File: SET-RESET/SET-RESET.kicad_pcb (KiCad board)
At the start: 2 copper layers, 100.1 x 100.1 mm, 107 parts, among them J1 BMS, J2 BSPD, J3 IMD, J4 IMD_SHTDNW, J5 BMS_SHTDNW, J6 BSPD_SHTDNW, J7 Led's paineis, J8 voltage supply, K1 RELAY_19.1x15.5mm, K2 RELAY_19.1x15.5mm, K3 RELAY_19.1x15.5mm, K4 RELAY_19.1x15.5mm, K5 RELAY_19.1x15.5mm, K6 RELAY_19.1x15.5mm, Q1 BC557, Q10 BC548, Q11 BC548, Q12 BC557, Q13 BC548, Q14 BC548, Q15 BC557, Q16 BC548, Q17 BC548, Q18 BC557, Q2 BC557, Q3 BC557, Q4 Si2302DS, Q5 Si2302DS, Q6 Si2302DS, Q7 BC548, Q8 BC548, Q9 BC548, U1 TLP290-4

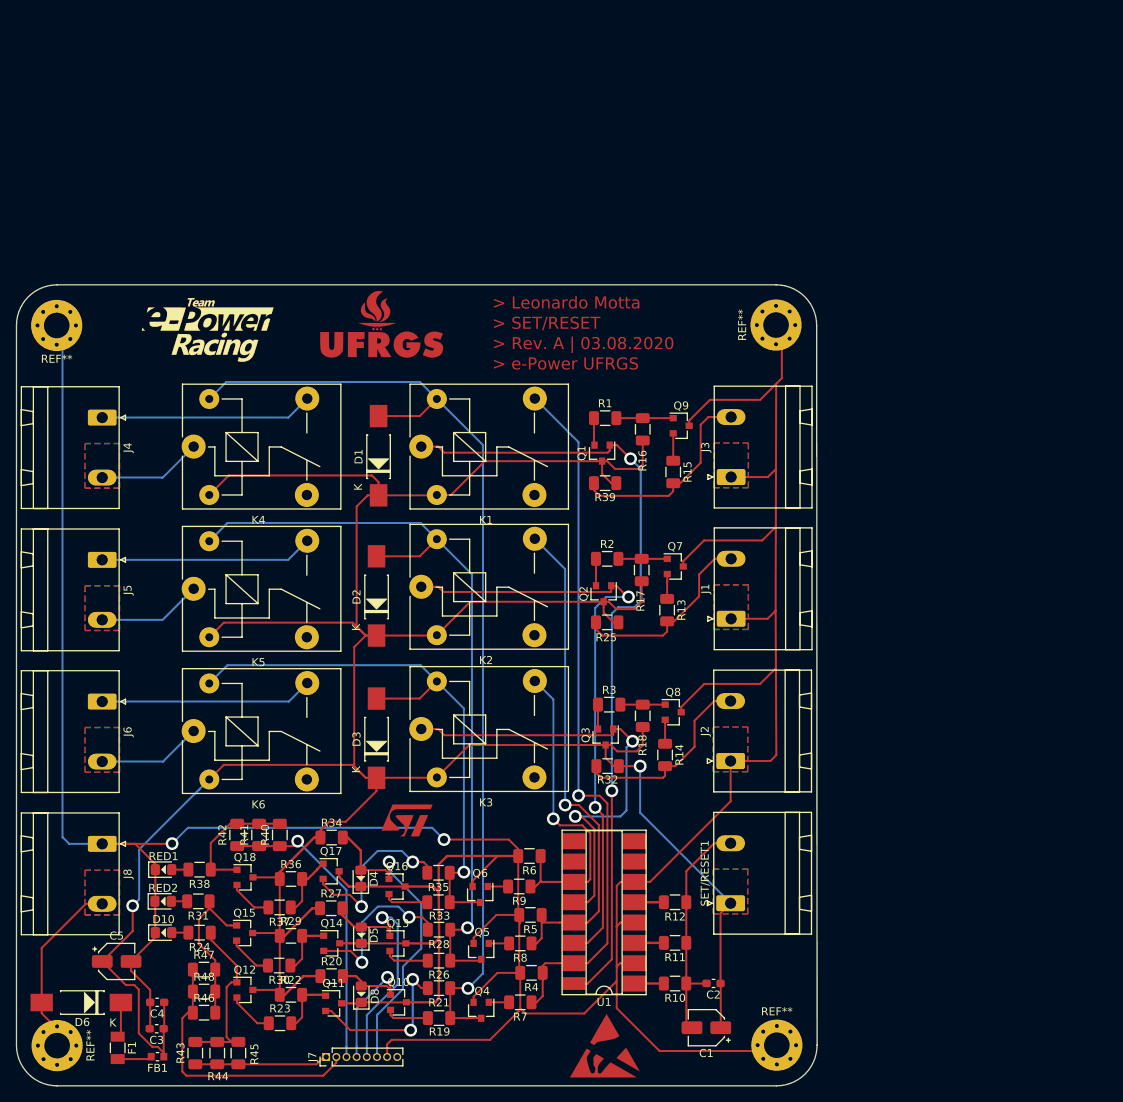
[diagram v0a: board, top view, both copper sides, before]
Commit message: Rev. B - BSPD and Rev. B - Set/Reset
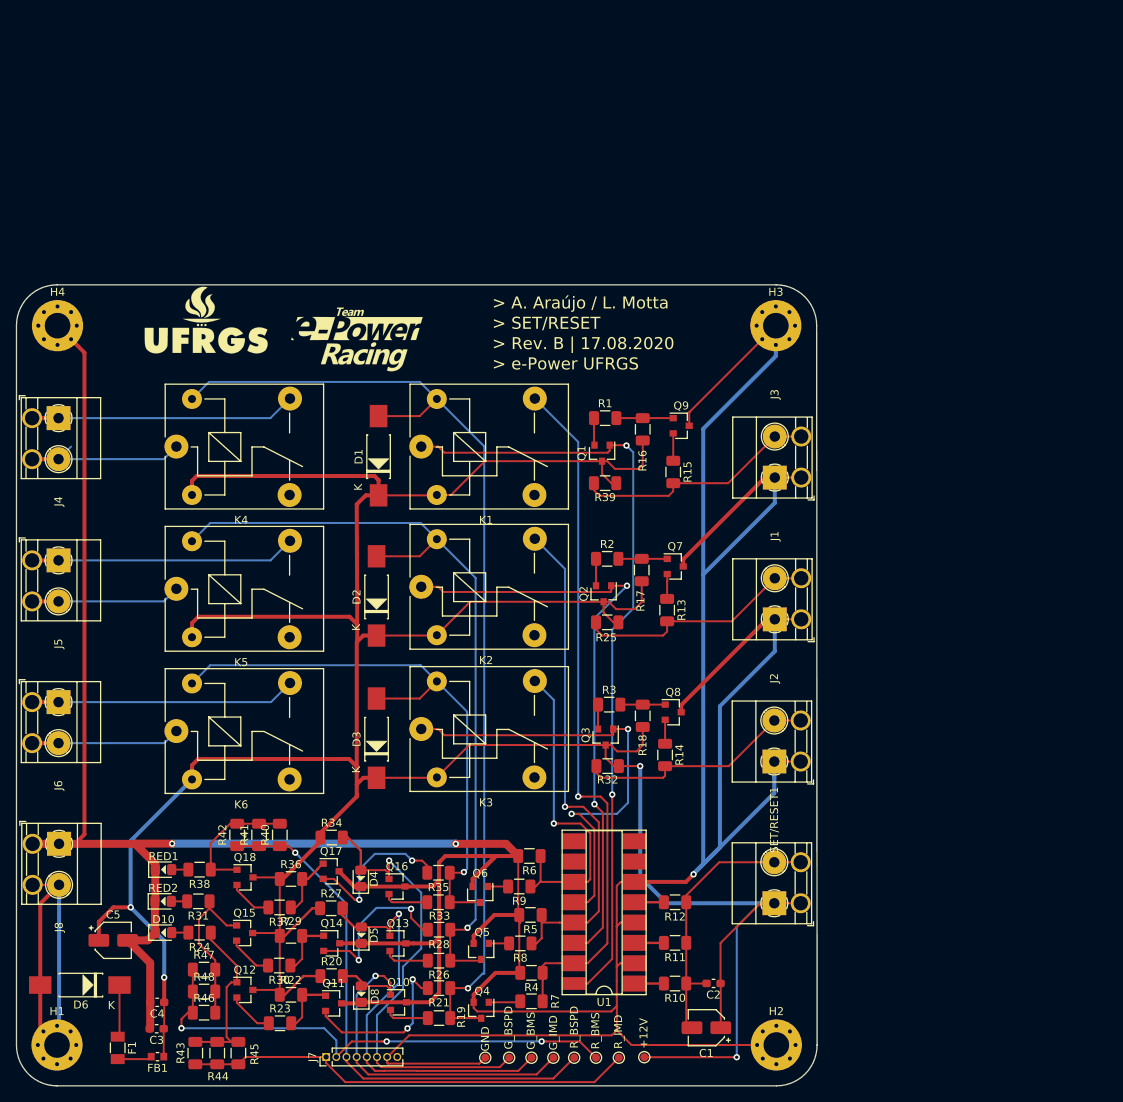
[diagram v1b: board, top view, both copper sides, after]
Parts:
- removed G3: ST Logo, e-Power:ST_6.5x4.1mm_Copper
- removed G4: UFRGS_1_14.7x8.0mm_Copper, e-Power:UFRGS_14.7x8.0mm_Copper
- removed REF** (x4): MountingHole_3.2mm_M3_Pad_Via, e-Power:MountingHole_3.2mm_M3_Pad_Via
- added G_BMS1: G_BMS, e-Power:TestPoint_Pad_D1.0mm, F.Cu at (177.4, 155.1)
- added G_BSPD1: G_BSPD, e-Power:TestPoint_Pad_D1.0mm, F.Cu at (174.6, 155.1)
- added G_IMD1: G_IMD, e-Power:TestPoint_Pad_D1.0mm, F.Cu at (180.1, 155.1)
- added H1: MountingHole_Pad, e-Power:MountingHole_3.2mm_M3_Pad_Via, F.Cu at (118.0, 153.5)
- added H2: MountingHole_Pad, e-Power:MountingHole_3.2mm_M3_Pad_Via, F.Cu at (208.0, 153.5)
- added H3: MountingHole_Pad, e-Power:MountingHole_3.2mm_M3_Pad_Via, F.Cu at (207.9, 63.6)
- added H4: MountingHole_Pad, e-Power:MountingHole_3.2mm_M3_Pad_Via, F.Cu at (118.1, 63.6)
- added R_BMS1: R_BMS, e-Power:TestPoint_Pad_D1.0mm, F.Cu at (185.4, 155.1)
- added R_BSPD1: R_BSPD, e-Power:TestPoint_Pad_D1.0mm, F.Cu at (182.7, 155.1)
- added R_IMD1: R_IMD, e-Power:TestPoint_Pad_D1.0mm, F.Cu at (188.3, 155.1)
- added TP1: GND, e-Power:TestPoint_Pad_D1.0mm, F.Cu at (171.6, 155.1)
- added TP2: +12V, e-Power:TestPoint_Pad_D1.0mm, F.Cu at (191.5, 155.1)
- C5: value 470uF -> 220uF
- G1: value e-Power_12.4x6.0mm_Copper -> Logo_e-Power_Large; footprint e-Power:e-Power_16.5x8.0mm_Copper -> e-Power:Logo_e-Power_16.5x8.0mm_SilkS
- G2: value UFRGS_1_11.0x6.0mm_Copper -> Logo_UFRGS_Large; footprint e-Power:ESD-Logo_8.9x8mm_Copper -> e-Power:Logo_UFRGS_14.7x8.0mm_SilkS
- J1, J2, J3, J4, J5, J6, J8, SET/RESET1: footprint Connector_Phoenix_GMSTB:PhoenixContact_GMSTBA_2,5_2-G_1x02_P7.50mm_Horizontal -> e-Power:TerminalBlock_Phoenix_MKDS-1,5-2_1x02_P5.08mm_Horizontal
- moved G2 103.5 mm to (136.7, 62.9)
- moved G1 18.7 mm to (155.5, 65.3)
- moved J4 5.46 mm to (118.2, 75.2)
- moved J5 5.46 mm to (118.2, 93.0)
- moved J6 5.46 mm to (118.2, 110.7)
- moved J1 5.46 mm to (207.8, 100.3)
- moved J2 5.46 mm to (207.7, 118.1)
- moved J3 5.46 mm to (207.8, 82.6)
- moved SET/RESET1 5.46 mm to (207.7, 135.8)
- moved J8 5.40 mm to (118.3, 128.4)
- moved C5 2.68 mm to (125.1, 140.5)
- moved D6 2.19 mm to (124.8, 146.1)
- moved K4 2.16 mm to (133.0, 78.7)
- moved K5 2.16 mm to (133.0, 96.5)
- moved K6 2.16 mm to (133.0, 114.3)
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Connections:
- D6 pad 2: +12V -> Input_Power
- J8 pad 2: +12V -> Input_Power
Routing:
- net GND: track 476.7 -> 587.9 mm, vias 2 -> 3
- net Input_Power: track 0.00 -> 44.9 mm
- net /ledRED_IMD: track 16.7 -> 56.3 mm
- net +12V: track 405.2 -> 435.3 mm, vias 2 -> 4
- net /ledRED_BMS: track 34.5 -> 64.5 mm, vias 0 -> 3
- net /ledRED_BSPD: track 37.3 -> 66.8 mm
- net /ledGREEN_IMD: track 21.5 -> 48.6 mm
- net /ledGREEN_BMS: track 30.8 -> 52.8 mm
- net /ledGREEN_BSPD: track 40.3 -> 58.5 mm
- net Net-(J5-Pad1): track 26.6 -> 35.4 mm
- net Net-(J4-Pad1): track 26.6 -> 35.4 mm
- net Net-(J6-Pad1): track 26.6 -> 35.4 mm
- net Net-(J4-Pad2): track 13.0 -> 20.9 mm
- net Net-(J1-Pad2): track 25.1 -> 31.4 mm
- net Net-(C1-Pad2): track 29.4 -> 35.4 mm
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- removed copper zone on B.Cu, net (none)
- removed copper zone on F.Cu, net (none)
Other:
- board text added: "> A. Araújo / L. Motta"
- board text added: "> Rev. B | 17.08.2020"
- board text removed: "> Leonardo Motta"
- board text removed: "> Rev. A | 03.08.2020"

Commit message: Set/Reset Rev. C
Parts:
- removed D10: RED, e-Power:LED_0805_1.15x1.40mm_HandSolder
- removed G_BMS1: G_BMS, e-Power:TestPoint_Pad_D1.0mm
- removed G_BSPD1: G_BSPD, e-Power:TestPoint_Pad_D1.0mm
- removed G_IMD1: G_IMD, e-Power:TestPoint_Pad_D1.0mm
- removed R40, R41, R42, R43, R44, R45, R46, R47, R48: 1K, Resistor_SMD:R_1206_3216Metric
- removed R_BMS1: R_BMS, e-Power:TestPoint_Pad_D1.0mm
- removed R_BSPD1: R_BSPD, e-Power:TestPoint_Pad_D1.0mm
- removed R_IMD1: R_IMD, e-Power:TestPoint_Pad_D1.0mm
- added RED3: RED, e-Power:LED_0805_1.15x1.40mm_HandSolder, F.Cu at (170.5, 121.0)
- added TP10: +VIN, e-Power:TestPoint_Pad_D1.0mm, F.Cu at (160.5, 123.4)
- added TP11: GND, e-Power:TestPoint_Pad_D1.0mm, F.Cu at (165.3, 123.4)
- added TP3: ERROR_BMS, e-Power:TestPoint_Pad_D1.0mm, F.Cu at (237.7, 40.2)
- added TP4: ERROR_IMD, e-Power:TestPoint_Pad_D1.0mm, F.Cu at (237.7, 37.9)
- added TP5: ERROR_BSPD, e-Power:TestPoint_Pad_D1.0mm, F.Cu at (237.8, 42.6)
- added TP7: Led_BSPD, e-Power:TestPoint_Pad_D1.0mm, F.Cu at (175.3, 114.2)
- added TP8: Led_IMD, e-Power:TestPoint_Pad_D1.0mm, F.Cu at (170.5, 114.2)
- added TP9: Led_BMS, e-Power:TestPoint_Pad_D1.0mm, F.Cu at (172.9, 114.2)
- C1, C5: footprint Capacitor_SMD:CP_Elec_4x5.3 -> Capacitor_SMD:CP_Elec_8x10
- C2, C3, C4: footprint Capacitor_SMD:C_0603_1608Metric_Pad1.05x0.95mm_HandSolder -> Capacitor_SMD:C_0805_2012Metric
- D1, D2, D3, D6: value 1N5819 -> SS54HF; footprint e-Power:DO-41_SMD -> e-Power:DO-214AC
- FB1: footprint e-Power:FB_0603_1608Metric -> e-Power:FB_0805_2012Metric
- Q1, Q12, Q15, Q18, Q2, Q3: value BC557 -> MMBT5551
- Q10, Q11, Q13, Q14, Q16, Q17, Q7, Q8, Q9: value BC548 -> MMBT5551
- R1, R10, R11, R12, R13, R14, R15, R16, R17, R18, R19, R2, R20, R21, R22, R23, R24, R25, R26, R27, R28, R29, R3, R30, R31, R32, R33, R34, R35, R36, R37, R38, R39, R4, R5, R6, R7, R8, R9: footprint Resistor_SMD:R_1206_3216Metric -> Resistor_SMD:R_0805_2012Metric
- U1: footprint e-Power:TLP290-4 -> e-Power:SOIC-16_4.55x10.3mm_P1.27mm(TLP290-4)
- moved H2 128.7 mm to (244.1, 30.1)
- moved TP1 128.4 mm to (237.8, 45.1), turned to 270 degrees
- moved J7 79.1 mm to (223.3, 121.5)
- moved Q3 75.3 mm to (223.6, 49.4), turned to 180 degrees
- moved Q12 69.6 mm to (203.0, 114.0)
- moved H3 67.0 mm to (244.2, 119.9)
- moved C1 60.6 mm to (242.9, 109.4), turned to 90 degrees
- moved Q10 58.4 mm to (203.1, 107.9)
- moved Q11 58.2 mm to (203.0, 119.3)
- moved F1 56.7 mm to (157.7, 107.1)
- moved FB1 56.1 mm to (160.2, 107.3), turned to 90 degrees
- moved Q15 56.1 mm to (190.9, 113.0), turned to 90 degrees
- moved C3 55.7 mm to (164.4, 107.3), turned to 90 degrees
- moved SET/RESET1 55.6 mm to (242.8, 92.8), turned to 270 degrees
- moved R39 54.3 mm to (229.0, 49.4), turned to 270 degrees
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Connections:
- D4 pad 2: /ledGREEN_BSPD -> Net-(D4-Pad2)
- D5 pad 2: /ledGREEN_BMS -> Net-(D5-Pad2)
- D8 pad 2: /ledGREEN_IMD -> Net-(D8-Pad2)
- J7 pad 1: /ledRED_IMD -> /led_IMD
- J7 pad 2: /ledRED_BMS -> /led_BMS
- J7 pad 3: /ledRED_BSPD -> /led_BSPD
- J7 pad 4: /ledGREEN_IMD -> Net-(J7-Pad4)
- J7 pad 5: /ledGREEN_BMS -> Net-(J7-Pad5)
- J7 pad 6: /ledGREEN_BSPD -> Net-(J7-Pad6)
- Q1 pad 1: Net-(K1-Pad1) -> Net-(Q1-Pad1)
- Q1 pad 2: Net-(Q1-Pad2) -> GND
- Q1 pad 3: +12V -> Net-(Q1-Pad3)
- Q10 pad 1: /ledGREEN_IMD -> Net-(Q10-Pad1)
- Q10 pad 2: Net-(Q10-Pad2) -> GND
- Q10 pad 3: GND -> Net-(D4-Pad2)
- Q11 pad 2: Net-(Q11-Pad2) -> GND
- Q11 pad 3: GND -> Net-(D8-Pad2)
- Q12 pad 2: Net-(Q12-Pad2) -> GND
- Q12 pad 3: +12V -> Net-(D5-Pad2)
- Q13 pad 1: /ledGREEN_BMS -> Net-(Q13-Pad1)
- Q13 pad 2: Net-(Q13-Pad2) -> GND
- Q13 pad 3: GND -> Net-(Q13-Pad3)
- Q14 pad 2: Net-(Q14-Pad2) -> GND
- Q14 pad 3: GND -> Net-(Q14-Pad3)
- Q15 pad 2: Net-(Q15-Pad2) -> GND
- Q15 pad 3: +12V -> Net-(Q15-Pad3)
- Q16 pad 1: /ledGREEN_BSPD -> Net-(Q16-Pad1)
- Q16 pad 2: Net-(Q16-Pad2) -> +12V
- Q16 pad 3: GND -> /led_BSPD
- Q17 pad 2: Net-(Q17-Pad2) -> +12V
- Q17 pad 3: GND -> /led_IMD
- Q18 pad 2: Net-(Q18-Pad2) -> +12V
- Q18 pad 3: +12V -> /led_BMS
- Q2 pad 1: Net-(K2-Pad1) -> Net-(Q2-Pad1)
- Q2 pad 2: Net-(Q2-Pad2) -> GND
- Q2 pad 3: +12V -> Net-(Q2-Pad3)
- Q3 pad 1: Net-(K3-Pad1) -> Net-(Q3-Pad1)
- Q3 pad 2: Net-(Q3-Pad2) -> GND
- Q3 pad 3: +12V -> Net-(Q3-Pad3)
- Q7 pad 2: Net-(Q7-Pad2) -> +12V
- Q7 pad 3: GND -> Net-(K1-Pad1)
- Q8 pad 2: Net-(Q8-Pad2) -> +12V
- Q8 pad 3: GND -> Net-(K2-Pad1)
- Q9 pad 2: Net-(Q9-Pad2) -> +12V
- Q9 pad 3: GND -> Net-(K3-Pad1)
- R1 pad 1: Net-(Q1-Pad2) -> Net-(Q7-Pad1)
- R1 pad 2: Net-(Q9-Pad1) -> Net-(Q3-Pad3)
- R13 pad 1: Net-(Q7-Pad2) -> Net-(Q1-Pad1)
- R14 pad 1: Net-(Q8-Pad2) -> Net-(Q2-Pad1)
- R15 pad 1: Net-(Q9-Pad2) -> Net-(Q3-Pad1)
- R16 pad 2: Net-(Q9-Pad1) -> Net-(Q3-Pad3)
- R17 pad 2: Net-(Q7-Pad1) -> Net-(Q1-Pad3)
- R18 pad 2: Net-(Q8-Pad1) -> Net-(Q2-Pad3)
- R19 pad 1: Net-(Q10-Pad2) -> Net-(Q11-Pad1)
- R2 pad 1: Net-(Q2-Pad2) -> Net-(Q8-Pad1)
- R2 pad 2: Net-(Q7-Pad1) -> Net-(Q1-Pad3)
- R20 pad 2: /ledGREEN_IMD -> Net-(D8-Pad2)
- R21 pad 2: Net-(Q11-Pad2) -> Net-(Q14-Pad1)
- R22 pad 2: Net-(Q11-Pad1) -> Net-(Q14-Pad3)
- R23 pad 1: Net-(Q12-Pad2) -> Net-(Q17-Pad1)
- R23 pad 2: Net-(Q11-Pad1) -> Net-(Q14-Pad3)
- R24 pad 1: Net-(Q12-Pad1) -> /led_IMD
- R26 pad 1: Net-(Q13-Pad2) -> Net-(Q12-Pad1)
- R27 pad 2: /ledGREEN_BMS -> Net-(D5-Pad2)
- R28 pad 1: Net-(Q14-Pad2) -> Net-(Q15-Pad1)
- R29 pad 2: Net-(Q14-Pad1) -> Net-(Q15-Pad3)
- R3 pad 1: Net-(Q3-Pad2) -> Net-(Q9-Pad1)
- R3 pad 2: Net-(Q8-Pad1) -> Net-(Q2-Pad3)
- R30 pad 1: Net-(Q14-Pad1) -> Net-(Q15-Pad3)
- R30 pad 2: Net-(Q15-Pad2) -> Net-(Q18-Pad1)
- R31 pad 1: Net-(Q15-Pad1) -> /led_BMS
- R33 pad 1: Net-(Q16-Pad2) -> Net-(Q10-Pad1)
- R34 pad 2: /ledGREEN_BSPD -> Net-(D4-Pad2)
- R35 pad 2: Net-(Q17-Pad2) -> Net-(Q13-Pad1)
- R36 pad 2: Net-(Q17-Pad1) -> Net-(Q13-Pad3)
- R37 pad 1: Net-(Q17-Pad1) -> Net-(Q13-Pad3)
- R37 pad 2: Net-(Q18-Pad2) -> Net-(Q16-Pad1)
- R38 pad 1: Net-(Q18-Pad1) -> /led_BSPD
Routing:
- net +12V: track 435.3 -> 551.5 mm, vias 4 -> 10
- net GND: track 587.9 -> 494.2 mm, vias 3 -> 12
- net /ledRED_BSPD: track 66.8 -> 0.00 mm, vias 1 -> 0
- net /ledRED_BMS: track 64.5 -> 0.00 mm, vias 3 -> 0
- net Net-(Q2-Pad1): track 0.00 -> 61.6 mm, vias 0 -> 2
- net /ledGREEN_BSPD: track 58.5 -> 0.00 mm, vias 1 -> 0
- net /ledRED_IMD: track 56.3 -> 0.00 mm
- net /ledGREEN_BMS: track 52.8 -> 0.00 mm, vias 1 -> 0
- net /ledGREEN_IMD: track 48.6 -> 0.00 mm, vias 1 -> 0
- net Net-(Q1-Pad1): track 0.00 -> 43.0 mm, vias 0 -> 2
- net Net-(Q3-Pad1): track 0.00 -> 26.9 mm
- net Net-(Q11-Pad2): track 20.9 -> 0.00 mm, vias 2 -> 0
- net /led_BSPD: track 0.00 -> 20.7 mm, vias 0 -> 2
- net Net-(Q14-Pad2): track 20.5 -> 0.00 mm, vias 2 -> 0
- net Net-(Q17-Pad2): track 20.2 -> 0.00 mm, vias 2 -> 0
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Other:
- board text added: "> Rev. C | 17.08.2020"
- board text removed: "> Rev. B | 17.08.2020"

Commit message: att set/reset and ail 07/09/2020
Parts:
- added J10: Painel, e-Power:TerminalBlock_Phoenix_MKDS-1,5-2_1x02_P5.08mm_Horizontal, F.Cu at (207.3, 119.4)
- added J11: Painel, e-Power:TerminalBlock_Phoenix_MKDS-1,5-2_1x02_P5.08mm_Horizontal, F.Cu at (218.4, 119.4)
- added J9: Painel, e-Power:TerminalBlock_Phoenix_MKDS-1,5-2_1x02_P5.08mm_Horizontal, F.Cu at (196.2, 119.4)
- added Q19: MMBT5551, Package_TO_SOT_SMD:SOT-23, F.Cu at (228.4, 122.4)
- added Q21: MMBT5551, Package_TO_SOT_SMD:SOT-23, F.Cu at (236.2, 122.4)
- added R40: 1K, Resistor_SMD:R_0805_2012Metric, F.Cu at (232.8, 118.6)
- added R41: 1K, Resistor_SMD:R_0805_2012Metric, F.Cu at (234.8, 118.6)
- added R42: 1K, Resistor_SMD:R_0805_2012Metric, F.Cu at (237.2, 118.6)
- added R6: 10K, Resistor_SMD:R_0805_2012Metric, F.Cu at (213.4, 98.5)
- J7: value Led's paineis -> Painel; footprint Connector_PinHeader_1.27mm:PinHeader_1x08_P1.27mm_Vertical -> e-Power:TerminalBlock_Phoenix_MKDS-1,5-2_1x02_P5.08mm_Horizontal
- Q20: renamed from R6; value 10K -> MMBT5551; footprint Resistor_SMD:R_0805_2012Metric -> Package_TO_SOT_SMD:SOT-23
- moved J7 38.2 mm to (185.2, 119.4), turned to 0 degrees
- moved Q20 21.4 mm to (232.2, 122.4), turned to 0 degrees
- moved Q11 9.36 mm to (199.0, 110.9)
- moved Q18 9.36 mm to (177.6, 100.7)
- moved Q4 9.36 mm to (207.6, 107.8)
- moved Q5 9.36 mm to (207.6, 103.9)
- moved Q6 9.36 mm to (207.6, 100.0)
- moved R20 9.36 mm to (191.7, 109.8)
- moved R22 9.36 mm to (182.5, 109.2)
- moved R23 9.36 mm to (182.5, 107.1)
- moved R26 9.36 mm to (203.3, 105.7)
- moved R9 9.36 mm to (213.4, 100.8)
- moved D4 9.36 mm to (194.8, 99.4)
- moved D5 9.36 mm to (194.8, 105.5)
- moved D8 9.36 mm to (194.8, 110.8)
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- renumbered H3 to GND, H2 to NC, H4 to NC, H1 to Vin+
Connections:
- NC pad 1: GND -> Net-(NC1-Pad1)
- NC pad 1: GND -> Net-(NC2-Pad1)
- Q20 pad 1: Net-(K3-Pad4) -> /led_BMS
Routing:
- net /led_IMD: track 19.4 -> 112.8 mm, vias 2 -> 3
- net /led_BMS: track 14.1 -> 98.0 mm, vias 0 -> 3
- net /led_BSPD: track 20.7 -> 87.2 mm, vias 2 -> 3
- net Net-(J9-Pad2): track 0.00 -> 48.3 mm
- net Net-(J10-Pad2): track 0.00 -> 44.1 mm, vias 0 -> 2
- net Net-(J10-Pad1): track 0.00 -> 43.9 mm, vias 0 -> 2
- net +12V: track 551.5 -> 589.4 mm
- net Net-(D1-Pad2): track 146.4 -> 134.9 mm
- net Net-(D2-Pad2): track 116.9 -> 106.9 mm
- net Net-(D3-Pad2): track 93.7 -> 84.8 mm
- net GND: track 494.2 -> 485.3 mm, vias 12 -> 16
- net Net-(K2-Pad4): track 65.4 -> 70.1 mm
- net Net-(K3-Pad4): track 43.2 -> 39.7 mm
- net Net-(J6-Pad1): track 30.1 -> 31.8 mm
- net Net-(J6-Pad2): track 16.3 -> 14.8 mm
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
